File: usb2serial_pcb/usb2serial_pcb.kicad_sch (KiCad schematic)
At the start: 29 parts, among them J1 USB_C_Receptacle_USB2.0, J2 DBUS, J3 UART1, J4 UART3, Q1 MMBT3904T, U1 XC6206P332MR, U2 STM32F103C8T6, Y1 Crystal_8M

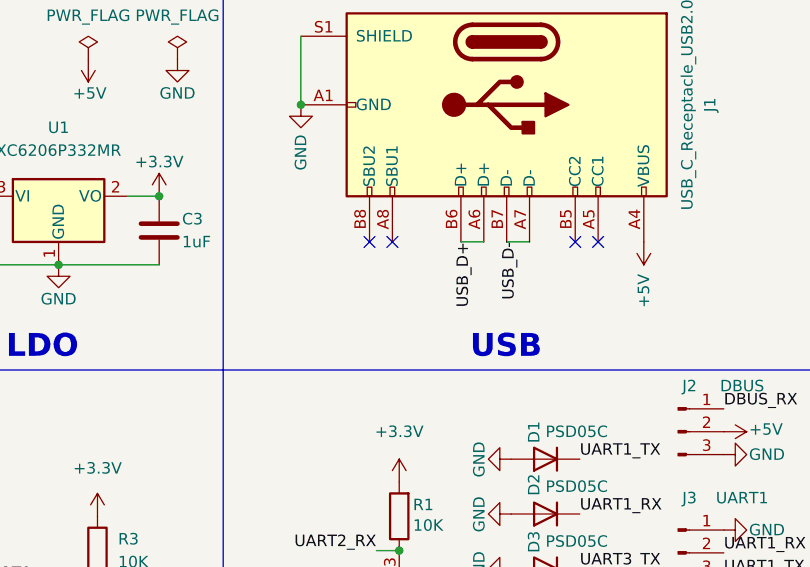
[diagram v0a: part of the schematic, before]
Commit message: add pull up register for USB enum
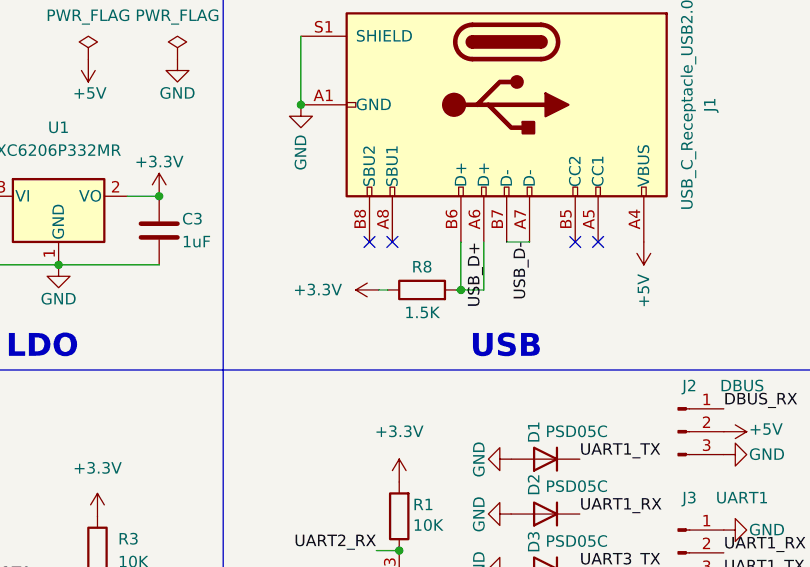
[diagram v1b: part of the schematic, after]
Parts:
- added R8: 1.5K, Resistor_SMD:R_0402_1005Metric, symbol Device:R
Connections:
- net +3.3V: now also R8.1
- net USB_D+: now also R8.2
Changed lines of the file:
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@@
   (junction (at 47.498 17.272) (diameter 0) (color 0 0 0 0)
+  )
+  (junction (at 157.988 45.72) (diameter 0) (color 0 0 0 0)
   )
   (junction (at 52.578 17.272) (diameter 0) (color 0 0 0 0)
@@
     (stroke (width 0) (type default) (color 0 0 0 0))
   )
+  (wire (pts (xy 148.844 45.72) (xy 149.86 45.72))
+    (stroke (width 0) (type default) (color 0 0 0 0))
+  )
   (wire (pts (xy 48.768 93.472) (xy 50.038 93.472))
     (stroke (width 0) (type default) (color 0 0 0 0))
@@
     (stroke (width 0) (type default) (color 0 0 0 0))
   )
+  (wire (pts (xy 157.988 40.386) (xy 157.988 45.72))
+    (stroke (width 0) (type default) (color 0 0 0 0))
+  )
   (polyline (pts (xy 49.276 103.886) (xy 49.276 136.144))
     (stroke (width 0) (type default) (color 0 0 0 0))
@@
     (stroke (width 0) (type default) (color 0 0 0 0))
   )
-  (wire (pts (xy 160.528 40.386) (xy 157.988 40.386))
-    (stroke (width 0) (type default) (color 0 0 0 0))
-  )
   (wire (pts (xy 97.282 78.232) (xy 104.14 78.232))
     (stroke (width 0) (type default) (color 0 0 0 0))
@@
     (stroke (width 0) (type default) (color 0 0 0 0))
   )
+  (wire (pts (xy 157.988 45.72) (xy 157.48 45.72))
+    (stroke (width 0) (type default) (color 0 0 0 0))
+  )
   (wire (pts (xy 73.152 113.03) (xy 73.152 115.062))
     (stroke (width 0) (type default) (color 0 0 0 0))
   )
+  (wire (pts (xy 160.528 45.72) (xy 157.988 45.72))
+    (stroke (width 0) (type default) (color 0 0 0 0))
+  )
   (polyline (pts (xy 131.572 11.938) (xy 131.572 103.886))
     (stroke (width 0) (type default) (color 0 0 0 0))
   )
   (wire (pts (xy 102.108 42.926) (xy 113.284 42.926))
+    (stroke (width 0) (type default) (color 0 0 0 0))
+  )
+  (wire (pts (xy 160.528 40.386) (xy 160.528 45.72))
     (stroke (width 0) (type default) (color 0 0 0 0))
   )
@@
     (effects (font (size 1.27 1.27)) (justify left bottom))
   )
-  (label "USB_D-" (at 164.338 40.386 270)
+  (label "USB_D-" (at 165.608 40.386 270)
     (effects (font (size 1.27 1.27)) (justify right bottom))
   )
@@
     (effects (font (size 1.27 1.27)) (justify left bottom))
   )
-  (label "USB_D+" (at 159.258 40.386 270)
+  (label "USB_D+" (at 160.528 40.386 270)
     (effects (font (size 1.27 1.27)) (justify right bottom))
   )
@@
     (pin "2")
   )
+  (symbol (lib_id "power:+3.3V") (at 148.844 45.72 90) (unit 1)
+    (in_bom yes) (on_board yes) (fields_autoplaced)
+    (property "Reference" "#PWR0101" (id 0) (at 152.654 45.72 0)
+      (effects (font (size 1.27 1.27)) hide)
+    )
+    (property "Value" "+3.3V" (id 1) (at 144.78 45.7199 90)
+      (effects (font (size 1.27 1.27)) (justify left))
+    )
+    (property "Footprint" "" (id 2) (at 148.844 45.72 0)
+      (effects (font (size 1.27 1.27)) hide)
+    )
+    (property "Datasheet" "" (id 3) (at 148.844 45.72 0)
+      (effects (font (size 1.27 1.27)) hide)
+    )
+    (pin "1")
+  )
   (symbol (lib_id "Device:D") (at 167.386 82.804 180) (unit 1)
     (in_bom yes) (on_board yes)
@@
     )
     (pin "1")
+  )
+  (symbol (lib_id "Device:R") (at 153.67 45.72 90) (unit 1)
+    (in_bom yes) (on_board yes)
+    (property "Reference" "R8" (id 0) (at 153.67 43.18 90))
+    (property "Value" "1.5K" (id 1) (at 153.67 48.26 90))
+    (property "Footprint" "Resistor_SMD:R_0402_1005Metric" (id 2) (at 153.67 47.498 90)
+      (effects (font (size 1.27 1.27)) hide)
+    )
+    (property "Datasheet" "~" (id 3) (at 153.67 45.72 0)
+      (effects (font (size 1.27 1.27)) hide)
+    )
+    (pin "1")
+    (pin "2")
   )
   (symbol (lib_id "power:GND") (at 113.284 42.926 0) (unit 1)
@@
       (reference "#PWR033") (unit 1) (value "+3.3V") (footprint "")
     )
+    (path "/503cbbb2-b92e-4cc2-89b8-ea74f053a6c6"
+      (reference "#PWR0101") (unit 1) (value "+3.3V") (footprint "")
+    )
     (path "/b3d0077e-9cac-454d-b5a0-9d3a3bf29ccb"
       (reference "C1") (unit 1) (value "0.1uF") (footprint "Capacitor_SMD:C_0402_1005Metric")
@@
       (reference "R7") (unit 1) (value "510R") (footprint "Resistor_SMD:R_0402_1005Metric")
     )
+    (path "/6f245bca-7382-43b9-b94e-73bd5025ba10"
+      (reference "R8") (unit 1) (value "1.5K") (footprint "Resistor_SMD:R_0402_1005Metric")
+    )
     (path "/5fc14624-14dc-40af-9cf8-c7acd716afa8"
